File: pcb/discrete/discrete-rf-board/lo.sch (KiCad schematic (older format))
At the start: 39 parts, among them J1601 Conn_Coaxial, J1602 Conn_Coaxial, Q1601 BFU520, U1601 ADF4360-7BCPZRL7, U1602 HHM17147A1

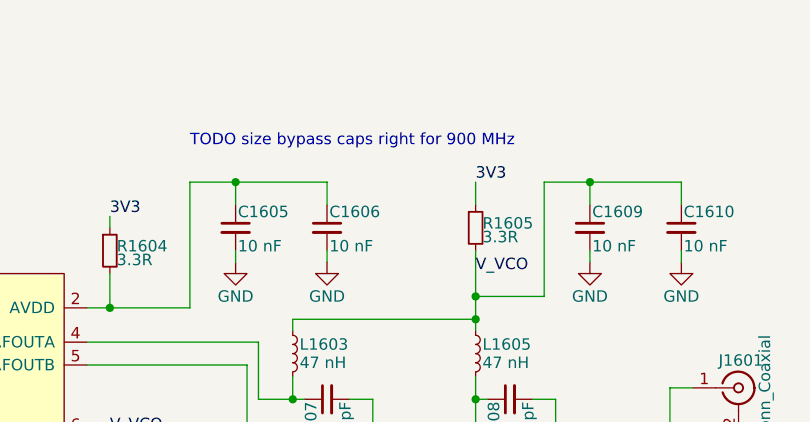
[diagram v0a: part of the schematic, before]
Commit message: Design DAC/ADC stages, pass out all control signals to top sheet
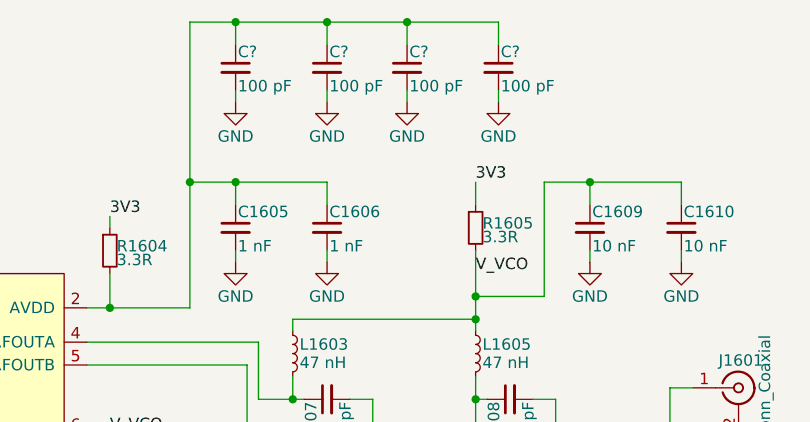
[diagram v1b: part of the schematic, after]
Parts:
- added C? (x4): 100 pF, symbol Device:C_Small
- C1605, C1606: value 10 nF -> 1 nF
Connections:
- net GND: now also C?.2, C?.2, C?.2, C?.2
- net at C1605.1, C1606.1, R1604.2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: now also C?.1, C?.1, C?.1, C?.1
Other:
- note removed: "TODO size bypass caps right for 900 MHz"
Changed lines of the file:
@@
 $Descr A4 11693 8268
 encoding utf-8
-Sheet 19 19
+Sheet 8 19
 Title ""
 Date ""
@@
 P 5400 2950
 F 0 "C1605" H 5410 3020 50  0000 L CNN
-F 1 "10 nF" H 5410 2870 50  0000 L CNN
+F 1 "1 nF" H 5410 2870 50  0000 L CNN
 F 2 "" H 5400 2950 50  0001 C CNN
 F 3 "~" H 5400 2950 50  0001 C CNN
@@
 P 5800 2950
 F 0 "C1606" H 5810 3020 50  0000 L CNN
-F 1 "10 nF" H 5810 2870 50  0000 L CNN
+F 1 "1 nF" H 5810 2870 50  0000 L CNN
 F 2 "" H 5800 2950 50  0001 C CNN
 F 3 "~" H 5800 2950 50  0001 C CNN
@@
 Wire Wire Line
 	6450 2750 6450 2850
-Text Notes 5200 2600 0    50   ~ 0
-TODO size bypass caps right for 900 MHz
 $Comp
 L Device:C_Small C1609
@@
 Text Notes 4800 4700 0    50   ~ 0
 TODO figure out loop filter\ncircuitry
+$Comp
+L Device:C_Small C?
+U 1 1 5DC21B18
+P 5400 2250
+F 0 "C?" H 5410 2320 50  0000 L CNN
+F 1 "100 pF" H 5410 2170 50  0000 L CNN
+F 2 "" H 5400 2250 50  0001 C CNN
+F 3 "~" H 5400 2250 50  0001 C CNN
+	1    5400 2250
+	1    0    0    -1
+$EndComp
+$Comp
+L Device:C_Small C?
+U 1 1 5DC21B1E
+P 5800 2250
+F 0 "C?" H 5810 2320 50  0000 L CNN
+F 1 "100 pF" H 5810 2170 50  0000 L CNN
+F 2 "" H 5800 2250 50  0001 C CNN
+F 3 "~" H 5800 2250 50  0001 C CNN
+	1    5800 2250
+	1    0    0    -1
+$EndComp
+Wire Wire Line
+	5800 2150 5800 2050
+Wire Wire Line
+	5800 2050 5400 2050
+Wire Wire Line
+	5400 2050 5400 2150
+Wire Wire Line
+	5400 2050 5200 2050
+Connection ~ 5400 2050
+$Comp
+L power:GND #PWR?
+U 1 1 5DC21B29
+P 5400 2400
+F 0 "#PWR?" H 5400 2150 50  0001 C CNN
+F 1 "GND" H 5400 2250 50  0000 C CNN
+F 2 "" H 5400 2400 50  0001 C CNN
+F 3 "" H 5400 2400 50  0001 C CNN
+	1    5400 2400
+	1    0    0    -1
+$EndComp
+$Comp
+L power:GND #PWR?
+U 1 1 5DC21B2F
+P 5800 2400
+F 0 "#PWR?" H 5800 2150 50  0001 C CNN
+F 1 "GND" H 5800 2250 50  0000 C CNN
+F 2 "" H 5800 2400 50  0001 C CNN
+F 3 "" H 5800 2400 50  0001 C CNN
+	1    5800 2400
+	1    0    0    -1
+$EndComp
+Wire Wire Line
+	5800 2400 5800 2350
+Wire Wire Line
+	5400 2350 5400 2400
+$Comp
+L Device:C_Small C?
+U 1 1 5DC2ABA4
+P 6150 2250
+F 0 "C?" H 6160 2320 50  0000 L CNN
+F 1 "100 pF" H 6160 2170 50  0000 L CNN
+F 2 "" H 6150 2250 50  0001 C CNN
+F 3 "~" H 6150 2250 50  0001 C CNN
+	1    6150 2250
+	1    0    0    -1
+$EndComp
+$Comp
+L Device:C_Small C?
+U 1 1 5DC2ABAA
+P 6550 2250
+F 0 "C?" H 6560 2320 50  0000 L CNN
+F 1 "100 pF" H 6560 2170 50  0000 L CNN
+F 2 "" H 6550 2250 50  0001 C CNN
+F 3 "~" H 6550 2250 50  0001 C CNN
+	1    6550 2250
+	1    0    0    -1
+$EndComp
+Wire Wire Line
+	6550 2150 6550 2050
+Wire Wire Line
+	6550 2050 6150 2050
+Wire Wire Line
+	6150 2050 6150 2150
+Connection ~ 6150 2050
+$Comp
+L power:GND #PWR?
+U 1 1 5DC2ABB5
+P 6150 2400
+F 0 "#PWR?" H 6150 2150 50  0001 C CNN
+F 1 "GND" H 6150 2250 50  0000 C CNN
+F 2 "" H 6150 2400 50  0001 C CNN
+F 3 "" H 6150 2400 50  0001 C CNN
+	1    6150 2400
+	1    0    0    -1
+$EndComp
+$Comp
+L power:GND #PWR?
+U 1 1 5DC2ABBB
+P 6550 2400
+F 0 "#PWR?" H 6550 2150 50  0001 C CNN
+F 1 "GND" H 6550 2250 50  0000 C CNN
+F 2 "" H 6550 2400 50  0001 C CNN
+F 3 "" H 6550 2400 50  0001 C CNN
+	1    6550 2400
+	1    0    0    -1
+$EndComp
+Wire Wire Line
+	6550 2400 6550 2350
+Wire Wire Line
+	6150 2350 6150 2400
+Wire Wire Line
+	5800 2050 6150 2050
+Connection ~ 5800 2050
+Wire Wire Line
+	5200 2050 5200 2750
+Connection ~ 5200 2750
 $EndSCHEMATC

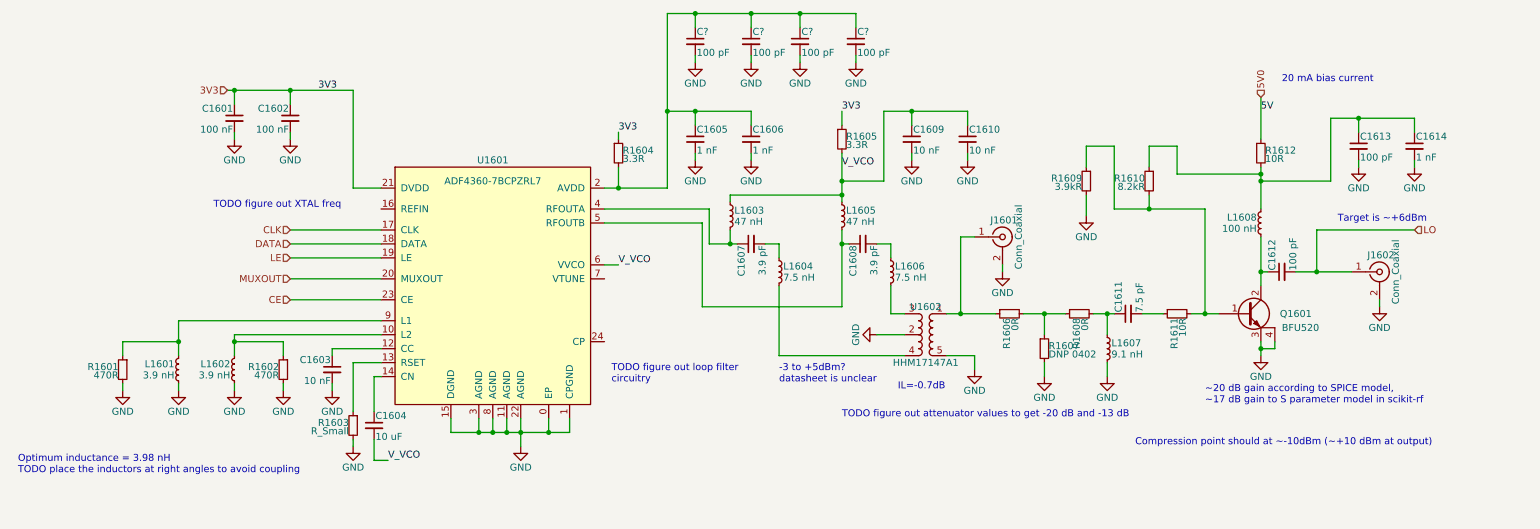
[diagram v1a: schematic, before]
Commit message: Wire out all control signals to connectors TODO PLL charge pump loop, bypass caps in attenuator circuit, antialiasing filter for ADC frontend
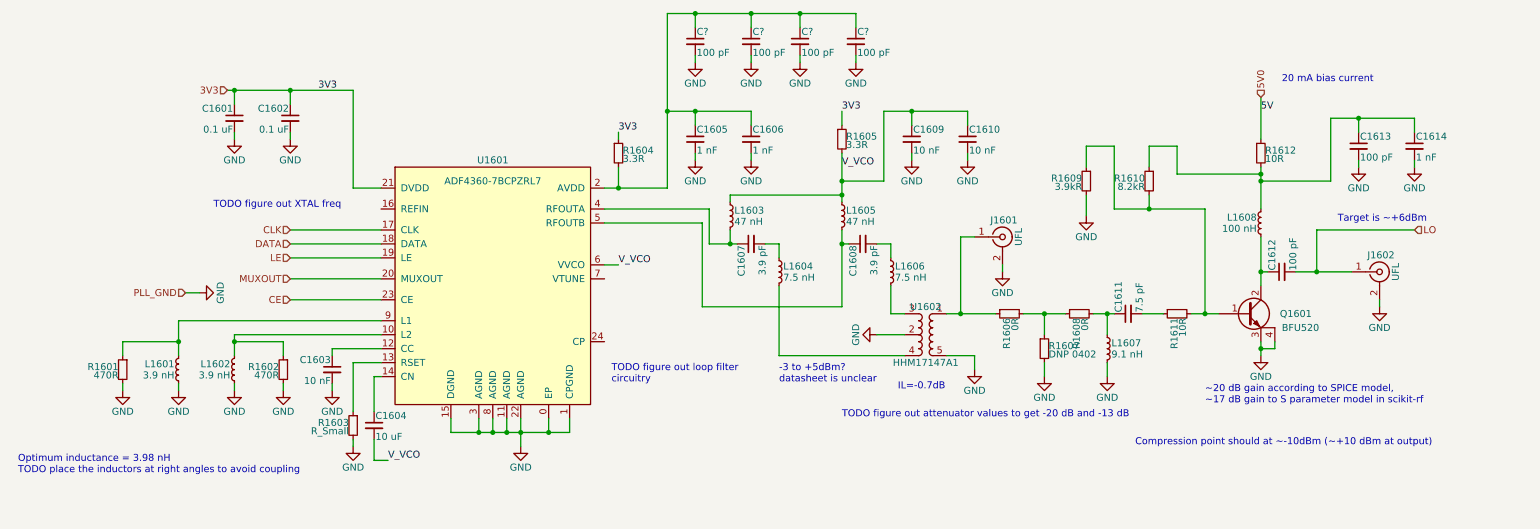
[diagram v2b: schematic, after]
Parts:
- C1601, C1602: value 100 nF -> 0.1 uF
- J1601, J1602: value Conn_Coaxial -> UFL
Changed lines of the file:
@@
 P 7600 3650
 F 0 "J1601" H 7610 3770 50  0000 C CNN
-F 1 "Conn_Coaxial" V 7715 3650 50  0000 C CNN
+F 1 "UFL" V 7715 3650 50  0000 C CNN
 F 2 "" H 7600 3650 50  0001 C CNN
 F 3 " ~" H 7600 3650 50  0001 C CNN
@@
 P 10300 3900
 F 0 "J1602" H 10310 4020 50  0000 C CNN
-F 1 "Conn_Coaxial" V 10415 3900 50  0000 C CNN
+F 1 "UFL" V 10415 3900 50  0000 C CNN
 F 2 "" H 10300 3900 50  0001 C CNN
 F 3 " ~" H 10300 3900 50  0001 C CNN
@@
 P 2500 2800
 F 0 "C1602" H 2510 2870 50  0000 L CNN
-F 1 "100 nF" H 2510 2720 50  0000 L CNN
+F 1 "0.1 uF" H 2510 2720 50  0000 L CNN
 F 2 "" H 2500 2800 50  0001 C CNN
 F 3 "~" H 2500 2800 50  0001 C CNN
@@
 P 2100 2800
 F 0 "C1601" H 2110 2870 50  0000 L CNN
-F 1 "100 nF" H 2110 2720 50  0000 L CNN
+F 1 "0.1 uF" H 2110 2720 50  0000 L CNN
 F 2 "" H 2100 2800 50  0001 C CNN
 F 3 "~" H 2100 2800 50  0001 C CNN
@@
 	5200 2050 5200 2750
 Connection ~ 5200 2750
+$Comp
+L power:GND #PWR?
+U 1 1 5D904674
+P 1850 4050
+F 0 "#PWR?" H 1850 3800 50  0001 C CNN
+F 1 "GND" H 1850 3900 50  0000 C CNN
+F 2 "" H 1850 4050 50  0001 C CNN
+F 3 "" H 1850 4050 50  0001 C CNN
+	1    1850 4050
+	0    -1   -1   0
+$EndComp
+Text HLabel 1750 4050 0    50   Input ~ 0
+PLL_GND
+Wire Wire Line
+	1750 4050 1850 4050
 $EndSCHEMATC

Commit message: Start work in footprinting everything
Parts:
- U1601: footprint (none) -> discrete_footprints:Analog_CP-24-14; Mouser (none) -> 584-ADF4360-7BCPZR7
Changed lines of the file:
@@
 F 0 "U1601" H 3950 4000 50  0000 C CNN
 F 1 "ADF4360-7BCPZRL7" H 3950 3850 50  0000 C CNN
-F 2 "" H 3950 3550 50  0001 C CNN
+F 2 "discrete_footprints:Analog_CP-24-14" H 3950 3550 50  0001 C CNN
 F 3 "" H 3950 3550 50  0001 C CNN
+F 4 " 584-ADF4360-7BCPZR7 " H 3950 3550 50  0001 C CNN "Mouser"
 	1    3950 3550
 	1    0    0    -1

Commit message: The footprintening continues
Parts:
- U1602: footprint (none) -> discrete_footprints:TDK_HHM17147A1
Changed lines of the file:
@@
 F 0 "U1602" H 7050 4550 50  0000 C CNN
 F 1 "HHM17147A1" H 7050 4150 50  0000 C CNN
-F 2 "" H 7050 4350 50  0001 C CNN
+F 2 "discrete_footprints:TDK_HHM17147A1" H 7050 4350 50  0001 C CNN
 F 3 "" H 7050 4350 50  0001 C CNN
 F 4 "810-HHM17147A1" H 7050 4350 50  0001 C CNN "Mouser"

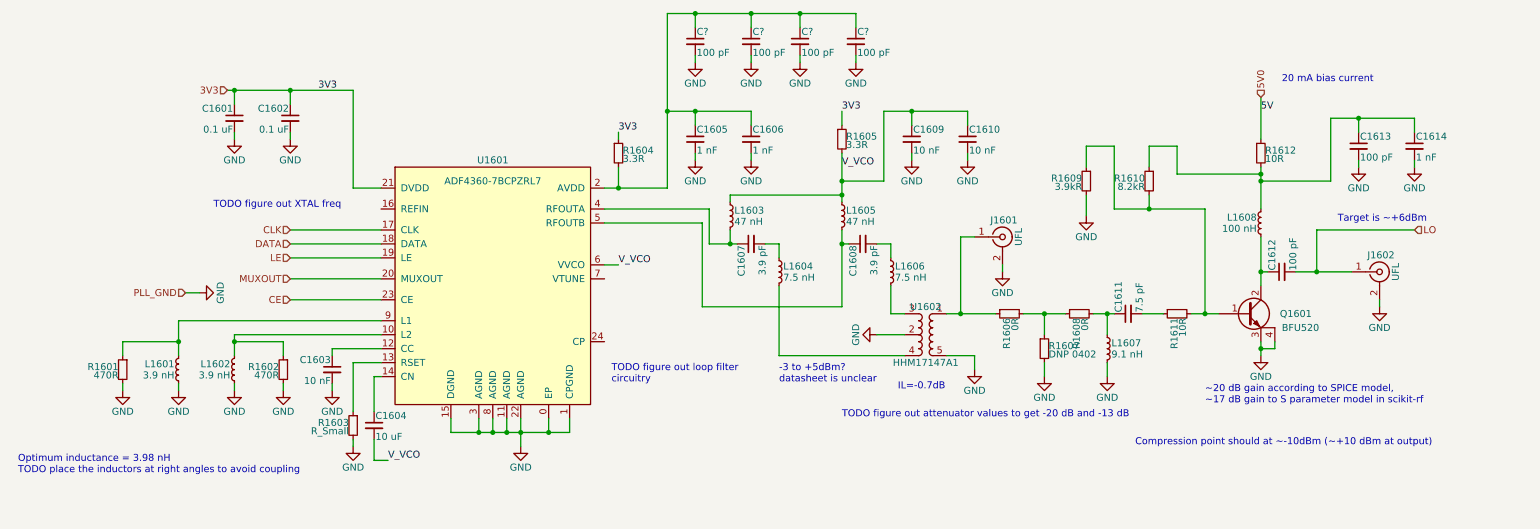
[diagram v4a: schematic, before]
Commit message: Add matching PNP/NPN transistor pairs, fix pin numbering for BFU520R transistors TODO fix biasing on power stage, source last NPN transistor, autofill and start sourcing passives
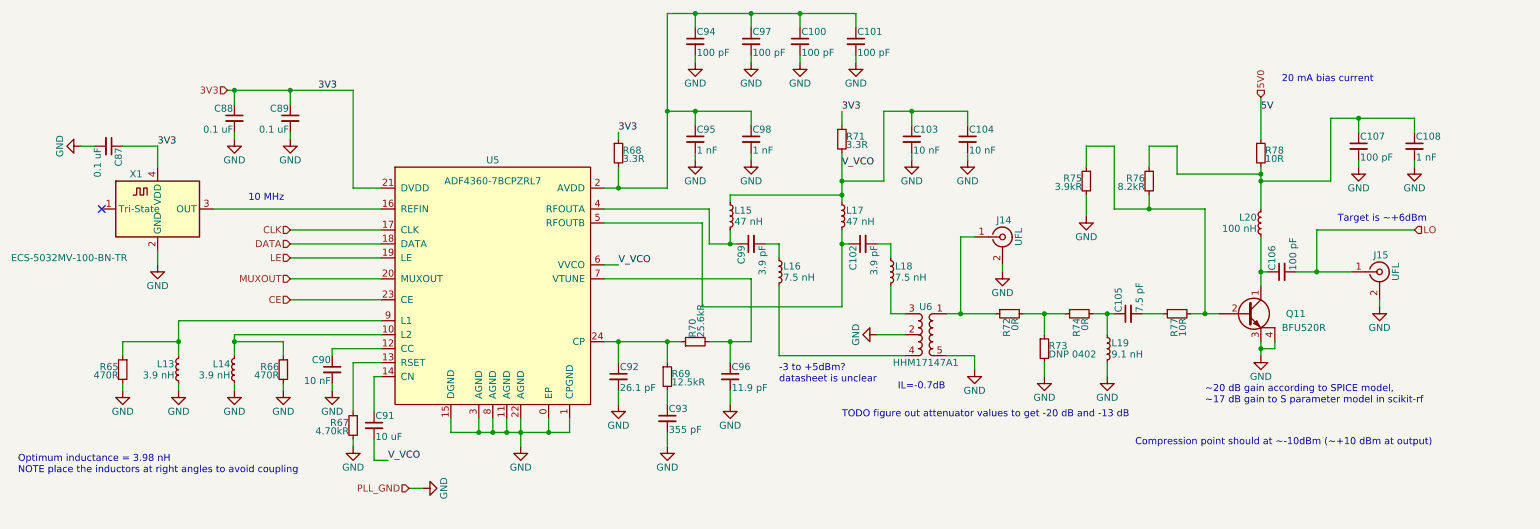
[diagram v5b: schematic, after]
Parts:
- removed Q1601: BFU520, symbol discrete-parts:Q_NPN_BCEE
- added C87: 0.1 uF, symbol Device:C_Small
- added C92: 26.1 pF, symbol Device:C_Small
- added C93: 355 pF, symbol Device:C_Small
- added C96: 11.9 pF, symbol Device:C_Small
- added Q11: BFU520R, symbol discrete-parts:Q_NPN_CBEE
- added R69: 12.5kR, symbol Device:R_Small
- added R70: 25.6kR, symbol Device:R_Small
- added X1: ECS-5032MV-100-BN-TR, Oscillator:Oscillator_SMD_EuroQuartz_XO53-4Pin_5.0x3.2mm_HandSoldering, symbol Oscillator:ECS-2520MV-xxx-xx
- R67: renamed from R1603; value R_Small -> 4.70kR
- gave numbers to parts that had none: 4
- renumbered C1608 to C102, C1609 to C103, C1610 to C104, C1611 to C105, C1612 to C106, C1613 to C107, C1614 to C108, C1601 to C88, C1602 to C89, C1603 to C90, C1604 to C91, C1605 to C95, C1606 to C98, C1607 to C99, J1601 to J14, J1602 to J15, L1601 to L13, L1602 to L14, L1603 to L15, L1604 to L16, L1605 to L17, L1606 to L18, L1607 to L19, L1608 to L20, R1601 to R65, R1602 to R66, R1604 to R68, R1605 to R71, R1606 to R72, R1607 to R73, R1608 to R74, R1609 to R75, R1610 to R76, R1611 to R77, R1612 to R78, U1601 to U5, U1602 to U6
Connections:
- net 3V3: now also C87.1, X1.4 (VDD)
- net GND: now also C87.2, C92.2, C93.2, C96.2, Q11.3 (E), Q11.4 (C), X1.2 (GND)
- net at U5.16 (REFIN): now also X1.3 (OUT)
- net at U5.24 (CP): now also C92.1, R69.1, R70.1
- net at U5.7 (VTUNE): now also C96.1, R70.2
- net at R75.1, R76.2, R77.2: now also Q11.2 (B)
- net at C106.1, L20.2: now also Q11.1 (C)
- new net: C93.1, R69.2
- no-connect marks 0 -> 1
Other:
- note added: "10 MHz"
- note added: "Optimum inductance = 3.98 nH\nNOTE place the inductors at right angles to avoid coupling"
- note removed: "Optimum inductance = 3.98 nH\nTODO place the inductors at right angles to avoid coupling"
- note removed: "TODO figure out XTAL freq"
- note removed: "TODO figure out loop filter\ncircuitry"

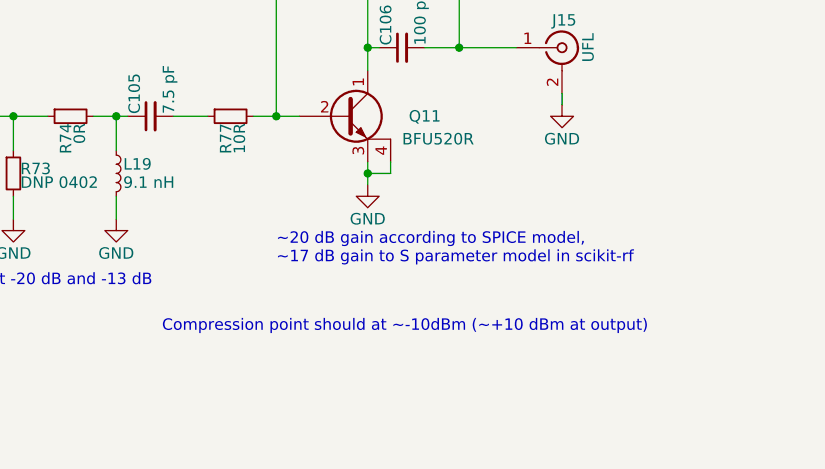
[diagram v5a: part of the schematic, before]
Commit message: All component values set (TODO change transistor gain stages to match values from experimentation
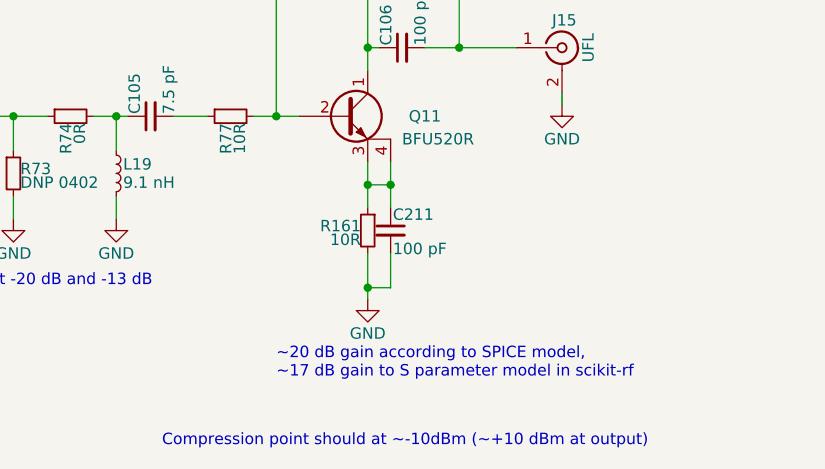
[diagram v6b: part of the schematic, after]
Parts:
- added C211: 100 pF, symbol Device:C_Small
- added R161: 10R, symbol Device:R_Small
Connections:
- net GND: now also C211.2, R161.2; no longer Q11.3 (E), Q11.4 (C)
- new net: C211.1, Q11.3 (E), Q11.4 (C), R161.1
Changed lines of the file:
@@
 L power:GND #PWR0127
 U 1 1 5CB0CCE1
-P 9450 4500
-F 0 "#PWR0127" H 9450 4250 50  0001 C CNN
-F 1 "GND" H 9450 4350 50  0000 C CNN
-F 2 "" H 9450 4500 50  0001 C CNN
-F 3 "" H 9450 4500 50  0001 C CNN
-	1    9450 4500
-	1    0    0    -1
-$EndComp
-Wire Wire Line
-	9450 4400 9450 4450
-Wire Wire Line
-	9550 4400 9550 4450
-Wire Wire Line
-	9550 4450 9450 4450
-Connection ~ 9450 4450
-Wire Wire Line
-	9450 4450 9450 4500
+P 9450 5000
+F 0 "#PWR0127" H 9450 4750 50  0001 C CNN
+F 1 "GND" H 9450 4850 50  0000 C CNN
+F 2 "" H 9450 5000 50  0001 C CNN
+F 3 "" H 9450 5000 50  0001 C CNN
+	1    9450 5000
+	1    0    0    -1
+$EndComp
+Wire Wire Line
+	9550 4950 9450 4950
+Connection ~ 9450 4950
+Wire Wire Line
+	9450 4950 9450 5000
 $Comp
 L Connector:Conn_Coaxial J14
@@
 Wire Wire Line
 	9450 3200 9450 3250
-Text Notes 9050 4850 0    50   ~ 0
+Text Notes 9050 5350 0    50   ~ 0
 ~~20 dB gain according to SPICE model,\n~~17 dB gain to S parameter model in scikit-rf
 Text Label 9450 2750 0    50   ~ 0
@@
 Text Notes 9600 2550 0    50   ~ 0
 20 mA bias current
-Text Notes 8550 5150 0    50   ~ 0
+Text Notes 8550 5650 0    50   ~ 0
 Compression point should at ~~-10dBm (~~+10 dBm at output)
 Text HLabel 9450 2650 1    50   Input ~ 0
@@
 	1    0    0    -1
 $EndComp
+Wire Wire Line
+	9450 4500 9550 4500
+Wire Wire Line
+	9550 4500 9550 4400
+$Comp
+L Device:R_Small R161
+U 1 1 5DAD826A
+P 9450 4700
+F 0 "R161" H 9480 4720 50  0000 L CNN
+F 1 "10R" H 9480 4660 50  0000 L CNN
+F 2 "" H 9450 4700 50  0001 C CNN
+F 3 "~" H 9450 4700 50  0001 C CNN
+	1    9450 4700
+	-1   0    0    -1
+$EndComp
+Wire Wire Line
+	9550 4800 9550 4950
+Wire Wire Line
+	9450 4800 9450 4950
+Wire Wire Line
+	9450 4400 9450 4500
+Connection ~ 9450 4500
+Wire Wire Line
+	9450 4500 9450 4600
+Wire Wire Line
+	9550 4500 9550 4600
+Connection ~ 9550 4500
+$Comp
+L Device:C_Small C211
+U 1 1 5DAD73DC
+P 9550 4700
+F 0 "C211" H 9560 4770 50  0000 L CNN
+F 1 "100 pF" H 9560 4620 50  0000 L CNN
+F 2 "" H 9550 4700 50  0001 C CNN
+F 3 "~" H 9550 4700 50  0001 C CNN
+	1    9550 4700
+	1    0    0    -1
+$EndComp

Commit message: Autofill; lots left to do
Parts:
- J14, J15: footprint (none) -> discrete_footprints:2337019-1; Mouser (none) -> 571-2337019-1
- Q11: footprint (none) -> discrete_footprints:NXP_SOT143B; Mouser (none) -> 771-BFU520R
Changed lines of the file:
@@
 F 0 "J14" H 7610 3770 50  0000 C CNN
 F 1 "UFL" V 7715 3650 50  0000 C CNN
-F 2 "" H 7600 3650 50  0001 C CNN
+F 2 "discrete_footprints:2337019-1" H 7600 3650 50  0001 C CNN
 F 3 " ~" H 7600 3650 50  0001 C CNN
+F 4 " 571-2337019-1" H 7600 3650 50  0001 C CNN "Mouser"
 	1    7600 3650
 	1    0    0    -1
@@
 F 0 "J15" H 10310 4020 50  0000 C CNN
 F 1 "UFL" V 10415 3900 50  0000 C CNN
-F 2 "" H 10300 3900 50  0001 C CNN
+F 2 "discrete_footprints:2337019-1" H 10300 3900 50  0001 C CNN
 F 3 " ~" H 10300 3900 50  0001 C CNN
+F 4 " 571-2337019-1" H 10300 3900 50  0001 C CNN "Mouser"
 	1    10300 3900
 	1    0    0    -1
@@
 F 0 "Q11" H 9700 4200 50  0000 C CNN
 F 1 "BFU520R" H 9600 4100 50  0000 L CNN
-F 2 "" H 9400 4200 50  0001 C CNN
+F 2 "discrete_footprints:NXP_SOT143B" H 9400 4200 50  0001 C CNN
 F 3 "" H 9400 4200 50  0001 C CNN
+F 4 " 771-BFU520R " H 9400 4200 50  0001 C CNN "Mouser"
 	1    9400 4200
 	1    0    0    -1

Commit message: Footprint some stuff
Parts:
- C97: footprint (none) -> Capacitor_SMD:C_0402_1005Metric; Mouser (none) -> 791-RF15N101J250CT
- R76: value 8.2kR -> 8k2R
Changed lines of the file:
@@
 P 8650 3250
 F 0 "R76" H 8680 3270 50  0000 L CNN
-F 1 "8.2kR" H 8680 3210 50  0000 L CNN
+F 1 "8k2R" H 8680 3210 50  0000 L CNN
 F 2 "" H 8650 3250 50  0001 C CNN
 F 3 "~" H 8650 3250 50  0001 C CNN
@@
 F 0 "C97" H 5810 2320 50  0000 L CNN
 F 1 "100 pF" H 5810 2170 50  0000 L CNN
-F 2 "" H 5800 2250 50  0001 C CNN
+F 2 "Capacitor_SMD:C_0402_1005Metric" H 5800 2250 50  0001 C CNN
 F 3 "~" H 5800 2250 50  0001 C CNN
+F 4 "791-RF15N101J250CT " H 5800 2250 50  0001 C CNN "Mouser"
 	1    5800 2250
 	1    0    0    -1
